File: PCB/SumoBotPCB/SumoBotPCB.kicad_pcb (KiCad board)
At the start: 2 copper layers, 90 x 62.5 mm, 27 parts, among them M1 Motor_DC, M2 Motor_DC, M3 Motor_DC, M4 Motor_DC, SW1 SW_Push, U1 TB6612FNG, U10 VL53L0X-GY530, U11 VL53L0X-GY530, U12 VL53L0X-GY530, U2 hc-05_BLUETOOTH_MODULE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

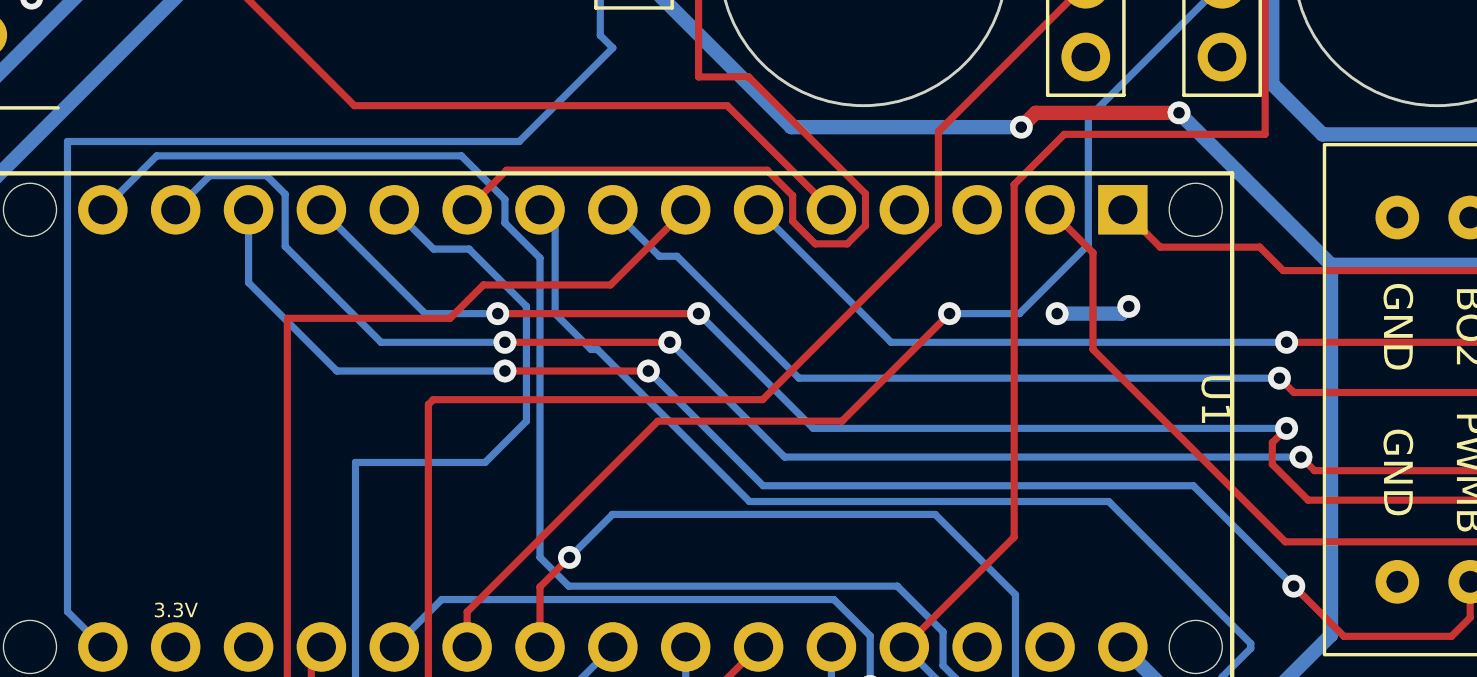
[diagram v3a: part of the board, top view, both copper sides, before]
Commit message: pwm groups change
d5 and d6 pwm operate at a different frequency than the rest
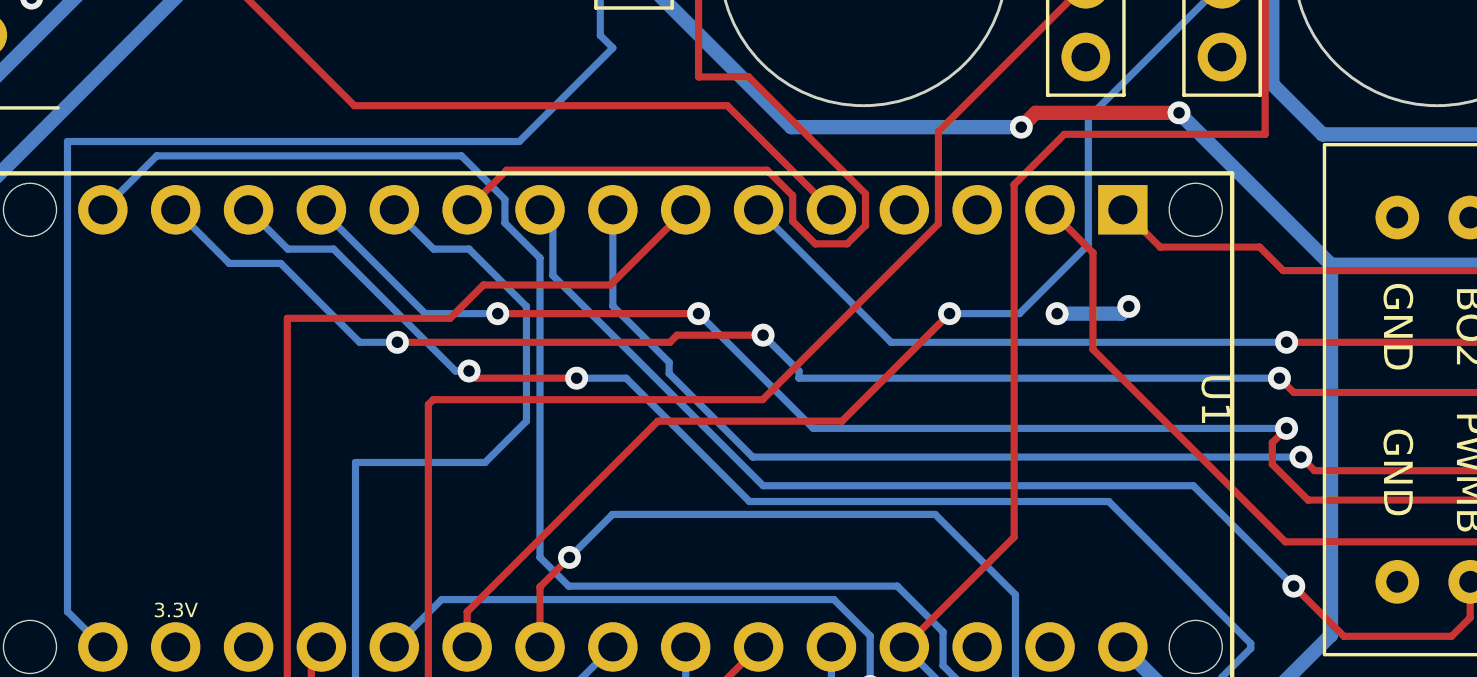
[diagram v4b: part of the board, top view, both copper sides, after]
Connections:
- U1 pad 10: Net-(U1-Pad10) -> Net-(XA1-PadD6)
- U1 pad 12: Net-(U1-Pad12) -> Net-(XA1-PadD10)
- U1 pad 14: Net-(U1-Pad14) -> Net-(XA1-PadD11)
- U1 pad 16: Net-(U1-Pad16) -> Net-(XA1-PadD5)
- XA1 pad D10: Net-(U1-Pad10) -> Net-(XA1-PadD10)
- XA1 pad D11: Net-(U1-Pad16) -> Net-(XA1-PadD11)
- XA1 pad D5: Net-(U1-Pad14) -> Net-(XA1-PadD5)
- XA1 pad D6: Net-(U1-Pad12) -> Net-(XA1-PadD6)
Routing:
- net Net-(U1-Pad16): track 70.3 -> 0.00 mm, vias 4 -> 0
- net Net-(XA1-PadD11): track 0.00 -> 64.3 mm, vias 0 -> 4
- net Net-(XA1-PadD10): track 0.00 -> 62.3 mm, vias 0 -> 3
- net Net-(XA1-PadD5): track 0.00 -> 55.2 mm, vias 0 -> 2
- net Net-(U1-Pad12): track 53.9 -> 0.00 mm, vias 1 -> 0
- net Net-(U1-Pad10): track 51.8 -> 0.00 mm, vias 3 -> 0
- net Net-(U1-Pad14): track 48.7 -> 0.00 mm, vias 2 -> 0
- net Net-(XA1-PadD6): track 0.00 -> 41.9 mm, vias 0 -> 1

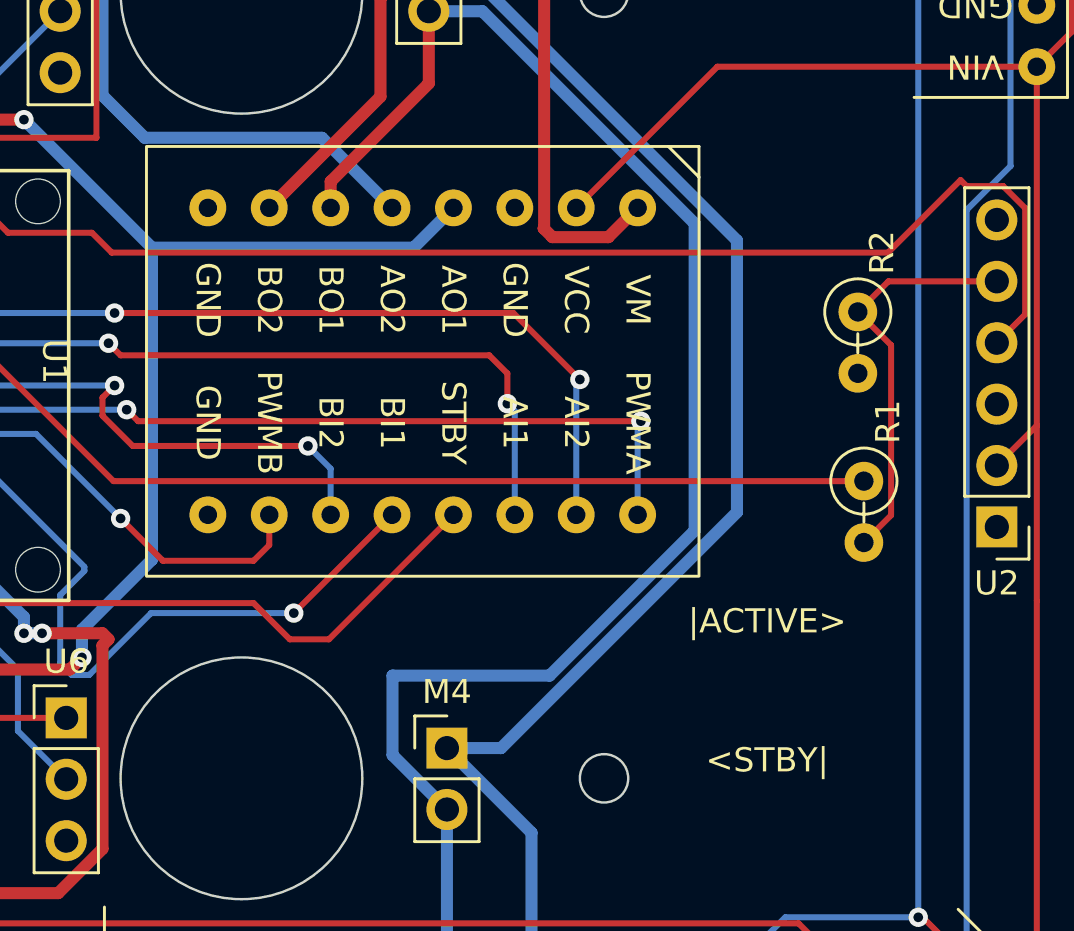
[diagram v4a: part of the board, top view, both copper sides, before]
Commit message: corrected driver foot print, add code
corrected footpring of motor driver from being 0.5" to 0.6"  and added the finalized code that works with arduino ide.
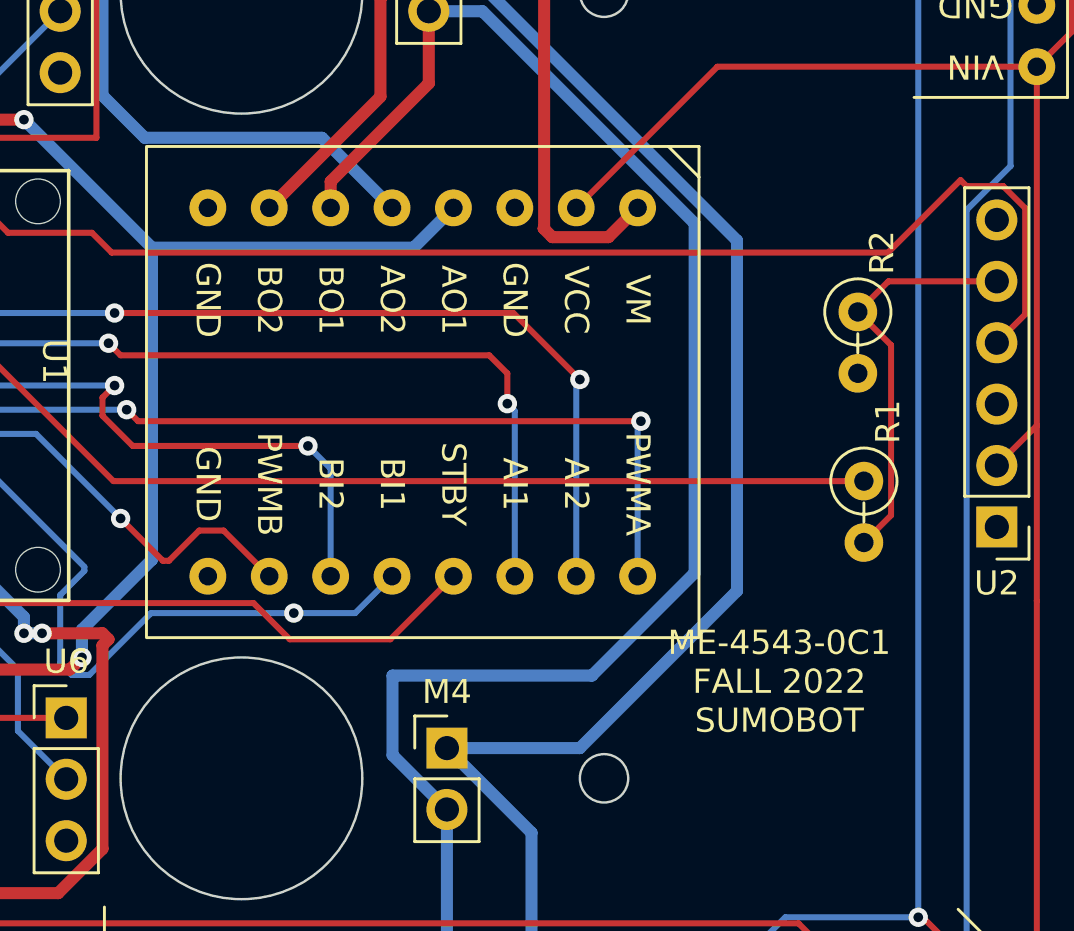
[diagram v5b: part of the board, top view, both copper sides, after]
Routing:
- net Net-(XA1-PadD3): track 46.4 -> 48.9 mm
- net Net-(U1-Pad14): track 64.3 -> 66.8 mm
- net Net-(U1-Pad11): track 50.5 -> 53.1 mm
- net Net-(XA1-PadD5): track 55.2 -> 57.6 mm
- net Net-(M2-Pad1): track 70.7 -> 72.6 mm
- net Net-(XA1-PadA1): track 50.9 -> 49.8 mm
- net Net-(XA1-PadD10): track 62.3 -> 61.2 mm
- net Net-(M2-Pad2): track 73.4 -> 74.4 mm
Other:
- board text added: "GROUP 18 JAMES MANLEY - ZTS530"
- board text added: "ME-4543-0C1 FALL 2022 SUMOBOT"
- board text removed: "<STBY|"
- board text removed: "|ACTIVE>"
